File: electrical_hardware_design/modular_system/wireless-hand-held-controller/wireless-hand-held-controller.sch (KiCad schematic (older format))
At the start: 54 parts, among them J1 328P_Prog_Pins, J2 328P_Bootloader_Pins, J3 Input Power, J4 2560_Prog_Pins, J5 2560_Bootloader_Pins, J6 Speaker Conn, J7 INT_PWR_CON, J8 External_Interrupts, U1 L7805CV, U2 AMS1117-3.3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

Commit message: add updated schematic file
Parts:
- U6: symbol wireless-control-lib:DRV2605L -> wireless-hand-held-controller-rescue:DRV2605L-wireless-control-lib
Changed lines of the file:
@@
 BNO055 Sensor
 $Comp
-L wireless-control-lib:DRV2605L U6
+L wireless-hand-held-controller-rescue:DRV2605L-wireless-control-lib U6
 U 1 1 60DDADC7
 P 10850 1850

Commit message: fix broken footprint import
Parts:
- removed U6: DRV2605L, wireless-hand-held-controller:DRV2605L, symbol wireless-hand-held-controller-rescue:DRV2605L-wireless-control-lib
- added U6: DRV2605L, wireless-hand-held-controller:DRV2605L, symbol wireless-control-lib:DRV2605L
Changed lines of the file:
@@
 BNO055 Sensor
-$Comp
-L wireless-hand-held-controller-rescue:DRV2605L-wireless-control-lib U6
-U 1 1 60DDADC7
-P 10850 1850
-F 0 "U6" H 11078 2171 50  0000 L CNN
-F 1 "DRV2605L" H 11078 2080 50  0000 L CNN
-F 2 "wireless-hand-held-controller:DRV2605L" H 10650 1850 50  0001 C CNN
-F 3 "" H 10650 1850 50  0001 C CNN
-	1    10850 1850
-	1    0    0    -1
-$EndComp
 $Comp
 L power:+5V #PWR0134
@@
 Wire Wire Line
 	7500 1550 7650 1550
+$Comp
+L wireless-control-lib:DRV2605L U6
+U 1 1 60ED77D3
+P 10850 1850
+F 0 "U6" H 11078 2171 50  0000 L CNN
+F 1 "DRV2605L" H 11078 2080 50  0000 L CNN
+F 2 "wireless-hand-held-controller:DRV2605L" H 10650 1850 50  0001 C CNN
+F 3 "" H 10650 1850 50  0001 C CNN
+	1    10850 1850
+	1    0    0    -1
+$EndComp
 $EndSCHEMATC

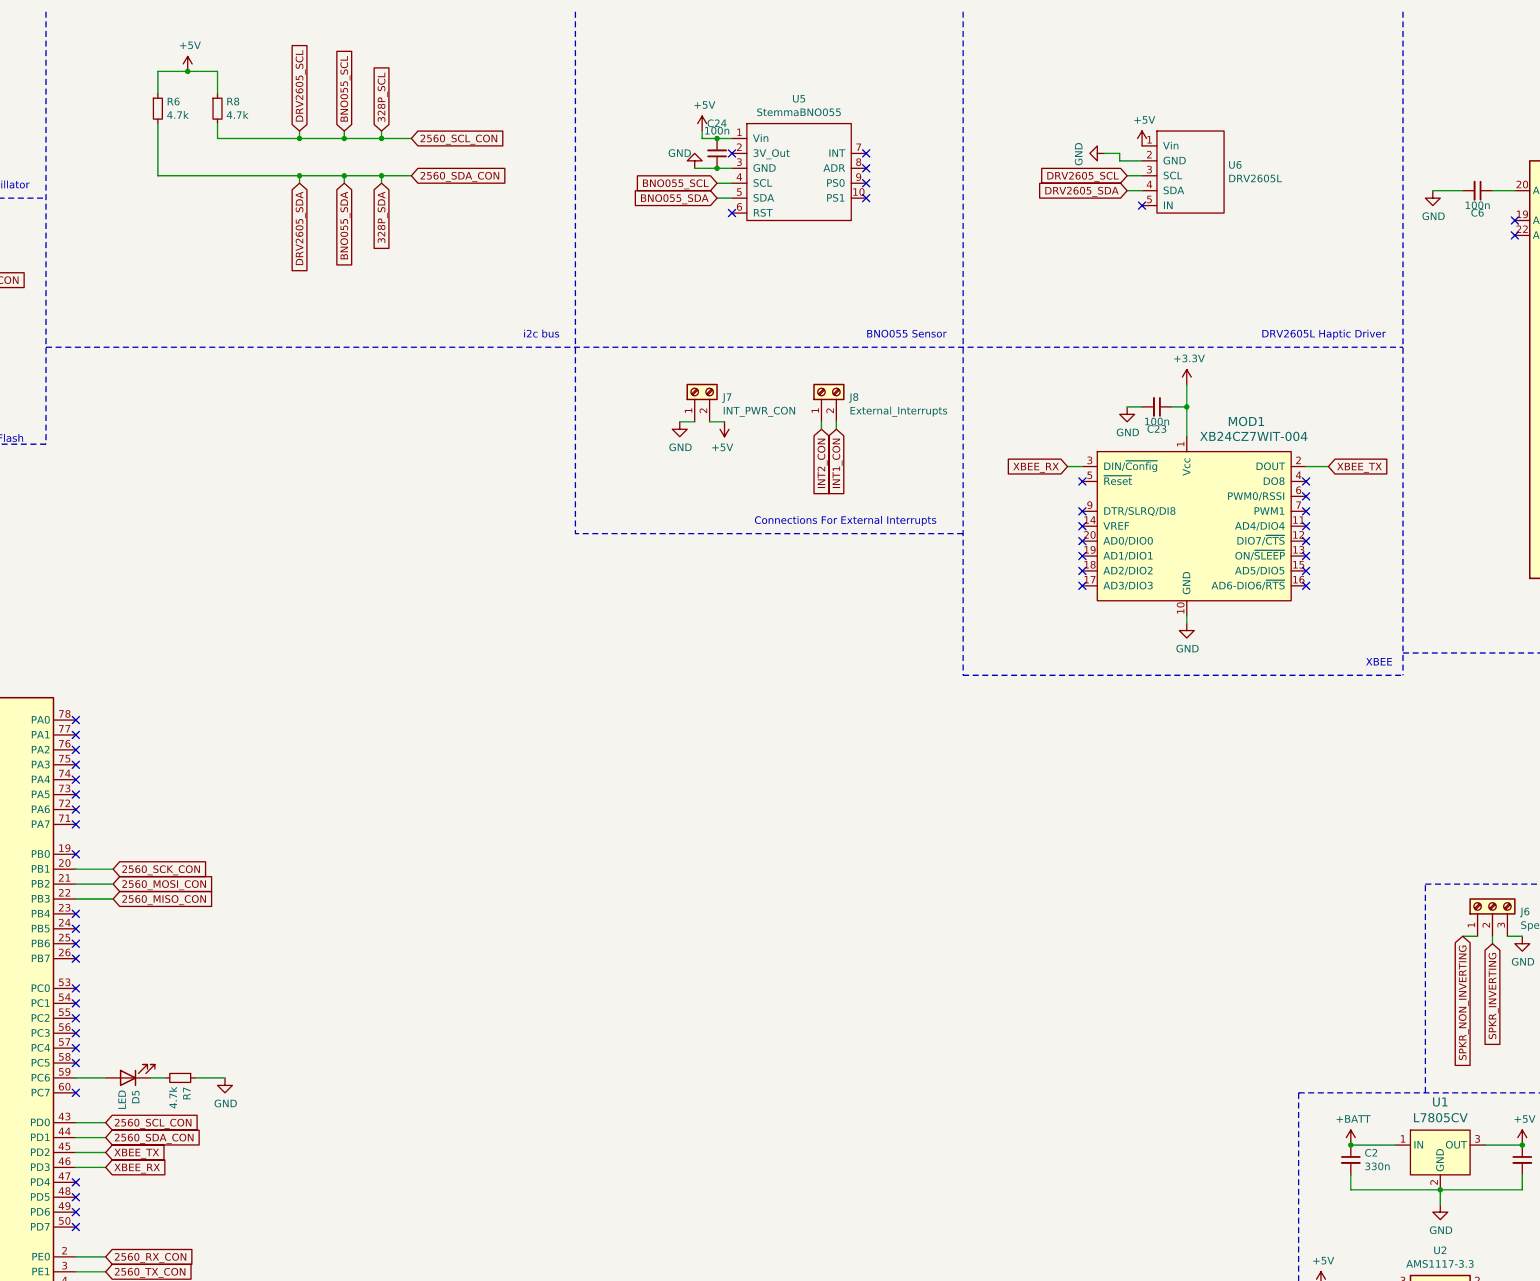
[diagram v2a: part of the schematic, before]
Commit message: add logic level shifters for xbee
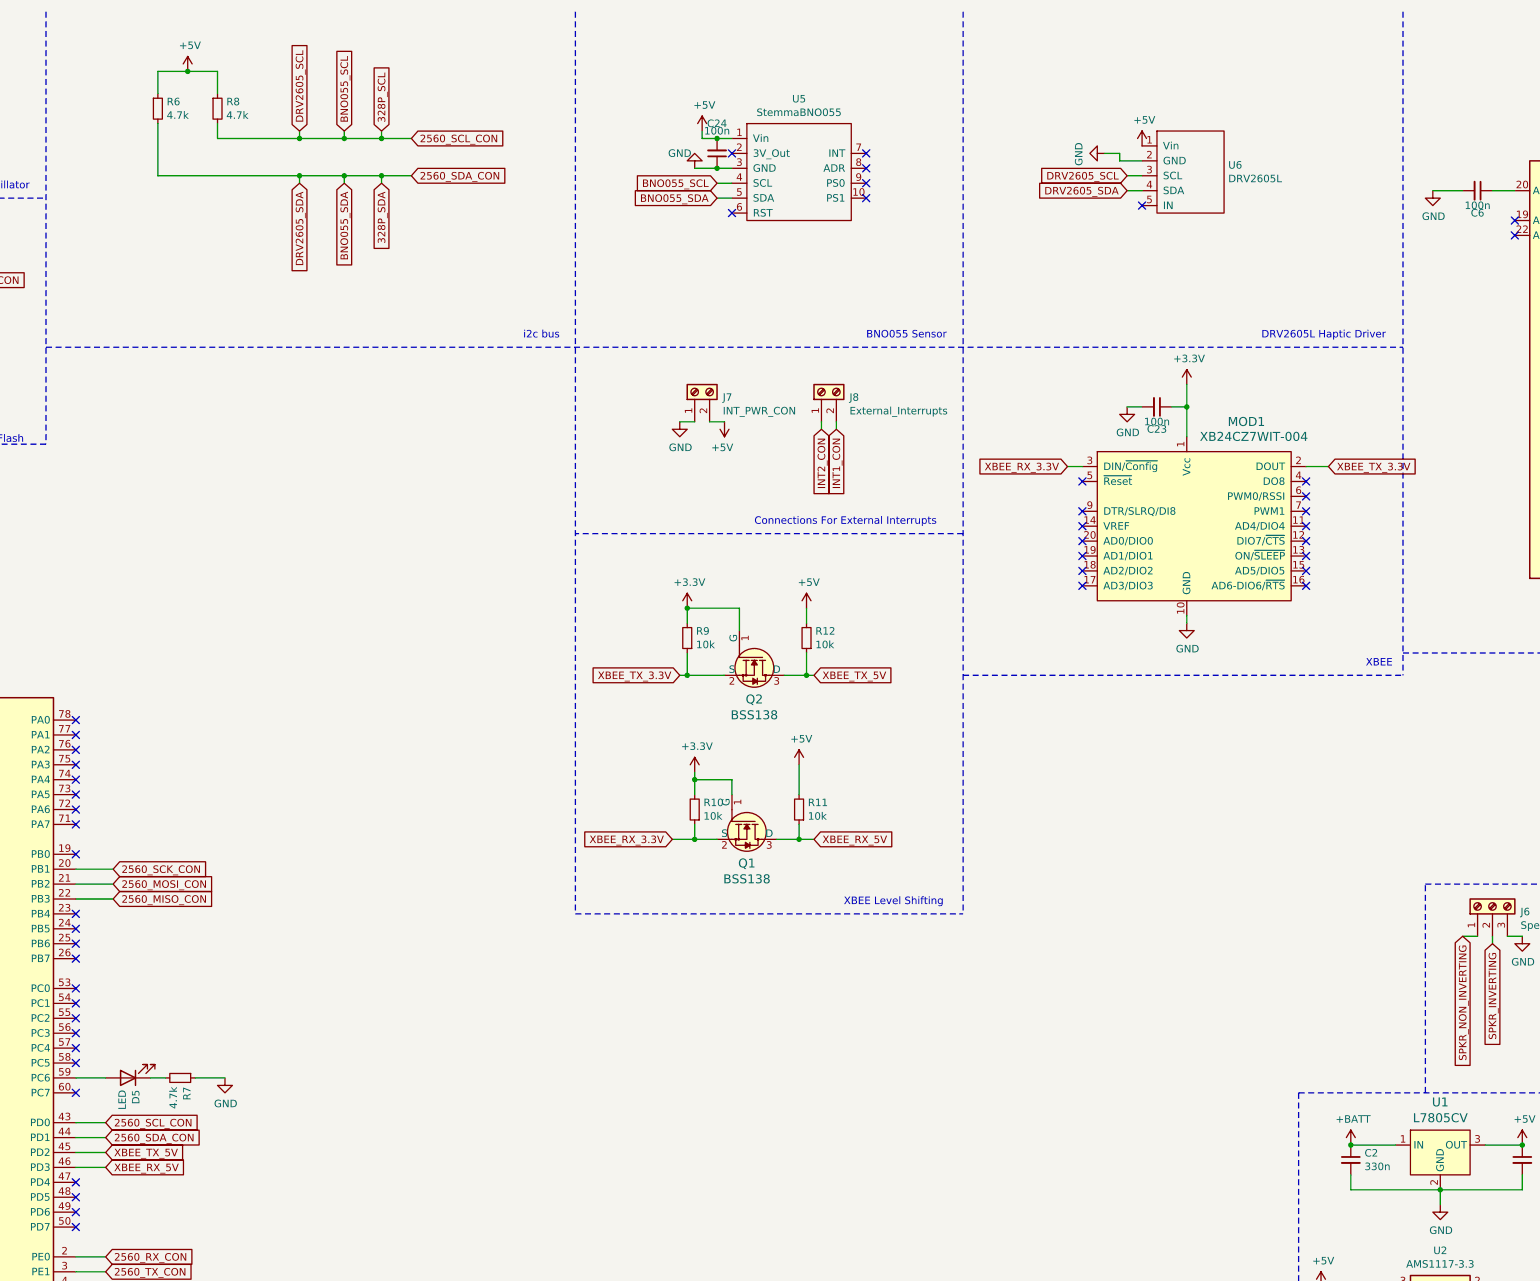
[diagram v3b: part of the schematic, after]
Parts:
- added Q1, Q2: BSS138, digikey-footprints:SOT-23-3, symbol dk_Transistors-FETs-MOSFETs-Single:BSS138
- added R10, R11, R12, R9: 10k, Resistor_SMD:R_1206_3216Metric, symbol Device:R_Small
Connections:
- net +3V3: now also Q1.1 (G), Q2.1 (G), R10.2, R9.2
- net +5V: now also R11.2, R12.2
- net XBEE_RX renamed XBEE_RX_3.3V
- net XBEE_RX_3.3V: now also Q1.2 (S), R10.1; no longer U4.46 (PD3)
- net XBEE_TX renamed XBEE_TX_3.3V
- net XBEE_TX_3.3V: now also Q2.2 (S), R9.1; no longer U4.45 (PD2)
- new net XBEE_RX_5V: Q1.3 (D), R11.1, U4.46 (PD3)
- new net XBEE_TX_5V: Q2.3 (D), R12.1, U4.45 (PD2)
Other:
- note added: "XBEE Level Shifting"
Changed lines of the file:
@@
 Connection ~ 13300 9050
-Wire Notes Line
-	11550 7750 11550 9600
-Wire Notes Line
-	11550 7750 16050 7750
 Wire Notes Line
 	11550 9600 16050 9600
@@
 	10000 3550 10100 3550
 Text GLabel 11750 3550 2    50   Input ~ 0
-XBEE_TX
+XBEE_TX_3.3V
 Wire Wire Line
 	11750 3550 11600 3550
@@
 NoConn ~ 11600 3650
 Text GLabel 10000 3550 0    50   Input ~ 0
-XBEE_RX
+XBEE_RX_3.3V
 Text GLabel 3550 8250 2    50   Input ~ 0
-XBEE_RX
+XBEE_RX_5V
 Text GLabel 3550 8150 2    50   Input ~ 0
-XBEE_TX
+XBEE_TX_5V
 Wire Wire Line
 	3550 8150 3350 8150
@@
 Wire Notes Line
 	9300 4950 12250 4950
-Wire Notes Line
-	12250 500  12250 4950
-Wire Notes Line
-	9300 500  9300 4950
 Text Notes 12000 4900 0    50   ~ 0
 XBEE
@@
 Wire Notes Line
 	9300 4000 6700 4000
-Wire Notes Line
-	6700 500  6700 4000
 Text Notes 7900 3950 0    50   ~ 0
 Connections For External Interrupts
@@
 	1    0    0    -1
 $EndComp
+$Comp
+L dk_Transistors-FETs-MOSFETs-Single:BSS138 Q2
+U 1 1 60F82E93
+P 7900 4950
+F 0 "Q2" V 8061 4950 60  0000 C CNN
+F 1 "BSS138" V 8167 4950 60  0000 C CNN
+F 2 "digikey-footprints:SOT-23-3" H 8100 5150 60  0001 L CNN
+F 3 "https://www.onsemi.com/pub/Collateral/BSS138-D.PDF" H 8100 5250 60  0001 L CNN
+F 4 "BSS138CT-ND" H 8100 5350 60  0001 L CNN "Digi-Key_PN"
+F 5 "BSS138" H 8100 5450 60  0001 L CNN "MPN"
+F 6 "Discrete Semiconductor Products" H 8100 5550 60  0001 L CNN "Category"
+F 7 "Transistors - FETs, MOSFETs - Single" H 8100 5650 60  0001 L CNN "Family"
+F 8 "https://www.onsemi.com/pub/Collateral/BSS138-D.PDF" H 8100 5750 60  0001 L CNN "DK_Datasheet_Link"
+F 9 "/product-detail/en/on-semiconductor/BSS138/BSS138CT-ND/244294" H 8100 5850 60  0001 L CNN "DK_Detail_Page"
+F 10 "MOSFET N-CH 50V 220MA SOT-23" H 8100 5950 60  0001 L CNN "Description"
+F 11 "ON Semiconductor" H 8100 6050 60  0001 L CNN "Manufacturer"
+F 12 "Active" H 8100 6150 60  0001 L CNN "Status"
+F 13 "C52895" V 7900 4950 50  0001 C CNN "LCSC"
+	1    7900 4950
+	0    1    1    0
+$EndComp
+Wire Notes Line
+	11550 7750 16050 7750
+Wire Notes Line
+	11550 7750 11550 9600
+$Comp
+L Device:R_Small R9
+U 1 1 60FA1024
+P 7450 4700
+F 0 "R9" H 7391 4654 50  0000 R CNN
+F 1 "10k" H 7391 4745 50  0000 R CNN
+F 2 "Resistor_SMD:R_1206_3216Metric" H 7450 4700 50  0001 C CNN
+F 3 "~" H 7450 4700 50  0001 C CNN
+F 4 "C17902" H 7450 4700 50  0001 C CNN "LCSC"
+	1    7450 4700
+	-1   0    0    1
+$EndComp
+Wire Wire Line
+	7450 4800 7450 4950
+Wire Wire Line
+	7450 4950 7700 4950
+Wire Wire Line
+	7800 4650 7800 4500
+Wire Wire Line
+	7800 4500 7450 4500
+Wire Wire Line
+	7450 4500 7450 4600
+$Comp
+L power:+3.3V #PWR0142
+U 1 1 60FEC4C3
+P 7450 4500
+F 0 "#PWR0142" H 7450 4350 50  0001 C CNN
+F 1 "+3.3V" H 7465 4673 50  0000 C CNN
+F 2 "" H 7450 4500 50  0001 C CNN
+F 3 "" H 7450 4500 50  0001 C CNN
+	1    7450 4500
+	1    0    0    -1
+$EndComp
+Connection ~ 7450 4500
+$Comp
+L Device:R_Small R12
+U 1 1 60FEDDDF
+P 8250 4700
+F 0 "R12" H 8191 4654 50  0000 R CNN
+F 1 "10k" H 8191 4745 50  0000 R CNN
+F 2 "Resistor_SMD:R_1206_3216Metric" H 8250 4700 50  0001 C CNN
+F 3 "~" H 8250 4700 50  0001 C CNN
+F 4 "C17902" H 8250 4700 50  0001 C CNN "LCSC"
+	1    8250 4700
+	-1   0    0    1
+$EndComp
+Wire Wire Line
+	8100 4950 8250 4950
+Wire Wire Line
+	8250 4950 8250 4800
+Wire Wire Line
+	8250 4600 8250 4500
+$Comp
+L power:+5V #PWR0143
+U 1 1 610083C0
+P 8250 4500
+F 0 "#PWR0143" H 8250 4350 50  0001 C CNN
+F 1 "+5V" H 8265 4673 50  0000 C CNN
+F 2 "" H 8250 4500 50  0001 C CNN
+F 3 "" H 8250 4500 50  0001 C CNN
+	1    8250 4500
+	1    0    0    -1
+$EndComp
+Wire Notes Line
+	12250 500  12250 4950
+Text GLabel 7400 4950 0    50   Input ~ 0
+XBEE_TX_3.3V
+Text GLabel 8300 4950 2    50   Input ~ 0
+XBEE_TX_5V
+Wire Wire Line
+	8300 4950 8250 4950
+Connection ~ 8250 4950
+Wire Wire Line
+	7400 4950 7450 4950
+Connection ~ 7450 4950
+Text GLabel 7350 6050 0    50   Input ~ 0
+XBEE_RX_3.3V
+Text GLabel 8300 6050 2    50   Input ~ 0
+XBEE_RX_5V
+$Comp
+L dk_Transistors-FETs-MOSFETs-Single:BSS138 Q1
+U 1 1 61062903
+P 7850 6050
+F 0 "Q1" V 8011 6050 60  0000 C CNN
+F 1 "BSS138" V 8117 6050 60  0000 C CNN
+F 2 "digikey-footprints:SOT-23-3" H 8050 6250 60  0001 L CNN
+F 3 "https://www.onsemi.com/pub/Collateral/BSS138-D.PDF" H 8050 6350 60  0001 L CNN
+F 4 "BSS138CT-ND" H 8050 6450 60  0001 L CNN "Digi-Key_PN"
+F 5 "BSS138" H 8050 6550 60  0001 L CNN "MPN"
+F 6 "Discrete Semiconductor Products" H 8050 6650 60  0001 L CNN "Category"
+F 7 "Transistors - FETs, MOSFETs - Single" H 8050 6750 60  0001 L CNN "Family"
+F 8 "https://www.onsemi.com/pub/Collateral/BSS138-D.PDF" H 8050 6850 60  0001 L CNN "DK_Datasheet_Link"
+F 9 "/product-detail/en/on-semiconductor/BSS138/BSS138CT-ND/244294" H 8050 6950 60  0001 L CNN "DK_Detail_Page"
+F 10 "MOSFET N-CH 50V 220MA SOT-23" H 8050 7050 60  0001 L CNN "Description"
+F 11 "ON Semiconductor" H 8050 7150 60  0001 L CNN "Manufacturer"
+F 12 "Active" H 8050 7250 60  0001 L CNN "Status"
+F 13 "C52895" V 7850 6050 50  0001 C CNN "LCSC"
+	1    7850 6050
+	0    1    1    0
+$EndComp
+Wire Wire Line
+	7350 6050 7500 6050
+Wire Wire Line
+	8050 6050 8200 6050
+$Comp
+L Device:R_Small R10
+U 1 1 6107BBBC
+P 7500 5850
+F 0 "R10" H 7441 5804 50  0000 R CNN
+F 1 "10k" H 7441 5895 50  0000 R CNN
+F 2 "Resistor_SMD:R_1206_3216Metric" H 7500 5850 50  0001 C CNN
+F 3 "~" H 7500 5850 50  0001 C CNN
+F 4 "C17902" H 7500 5850 50  0001 C CNN "LCSC"
+	1    7500 5850
+	-1   0    0    1
+$EndComp
+$Comp
+L Device:R_Small R11
+U 1 1 6107C1C7
+P 8200 5850
+F 0 "R11" H 8141 5804 50  0000 R CNN
+F 1 "10k" H 8141 5895 50  0000 R CNN
+F 2 "Resistor_SMD:R_1206_3216Metric" H 8200 5850 50  0001 C CNN
+F 3 "~" H 8200 5850 50  0001 C CNN
+F 4 "C17902" H 8200 5850 50  0001 C CNN "LCSC"
+	1    8200 5850
+	-1   0    0    1
+$EndComp
+Wire Wire Line
+	7500 5950 7500 6050
+Connection ~ 7500 6050
+Wire Wire Line
+	7500 6050 7650 6050
+Wire Wire Line
+	8200 5950 8200 6050
+Connection ~ 8200 6050
+Wire Wire Line
+	8200 6050 8300 6050
+$Comp
+L power:+3.3V #PWR0144
+U 1 1 61096AD1
+P 7500 5600
+F 0 "#PWR0144" H 7500 5450 50  0001 C CNN
+F 1 "+3.3V" H 7515 5773 50  0000 C CNN
+F 2 "" H 7500 5600 50  0001 C CNN
+F 3 "" H 7500 5600 50  0001 C CNN
+	1    7500 5600
+	1    0    0    -1
+$EndComp
+Wire Wire Line
+	7500 5750 7500 5650
+Wire Wire Line
+	7750 5750 7750 5650
+Wire Wire Line
+	7750 5650 7500 5650
+Connection ~ 7500 5650
+Wire Wire Line
+	7500 5650 7500 5600
+$Comp
+L power:+5V #PWR0145
+U 1 1 610B1586
+P 8200 5550
+F 0 "#PWR0145" H 8200 5400 50  0001 C CNN
+F 1 "+5V" H 8215 5723 50  0000 C CNN
+F 2 "" H 8200 5550 50  0001 C CNN
+F 3 "" H 8200 5550 50  0001 C CNN
+	1    8200 5550
+	1    0    0    -1
+$EndComp
+Wire Wire Line
+	8200 5750 8200 5550
+Wire Notes Line
+	6700 6550 9300 6550
+Wire Notes Line
+	9300 500  9300 6550
+Wire Notes Line
+	6700 500  6700 6550
+Text Notes 8500 6500 0    50   ~ 0
+XBEE Level Shifting
 $EndSCHEMATC
